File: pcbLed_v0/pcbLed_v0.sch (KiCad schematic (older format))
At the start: 16 parts, among them IC1 SN74AHCT125N, J1 Conn_01x02_Male

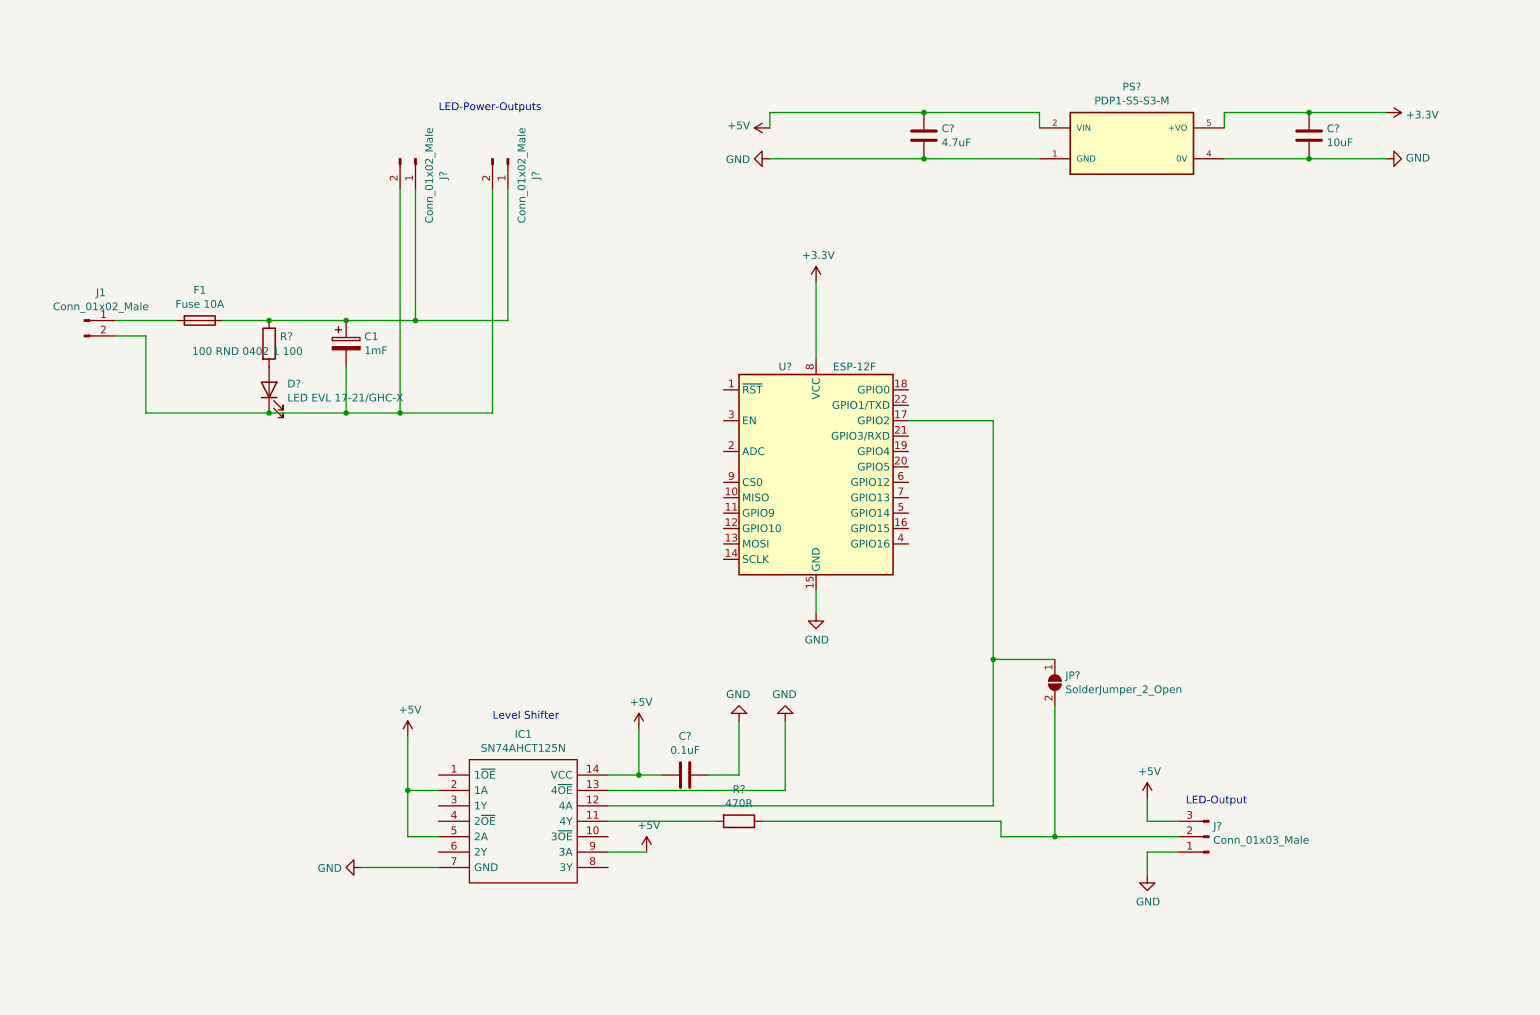
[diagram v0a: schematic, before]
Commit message: prototyp with full power supply through pcb
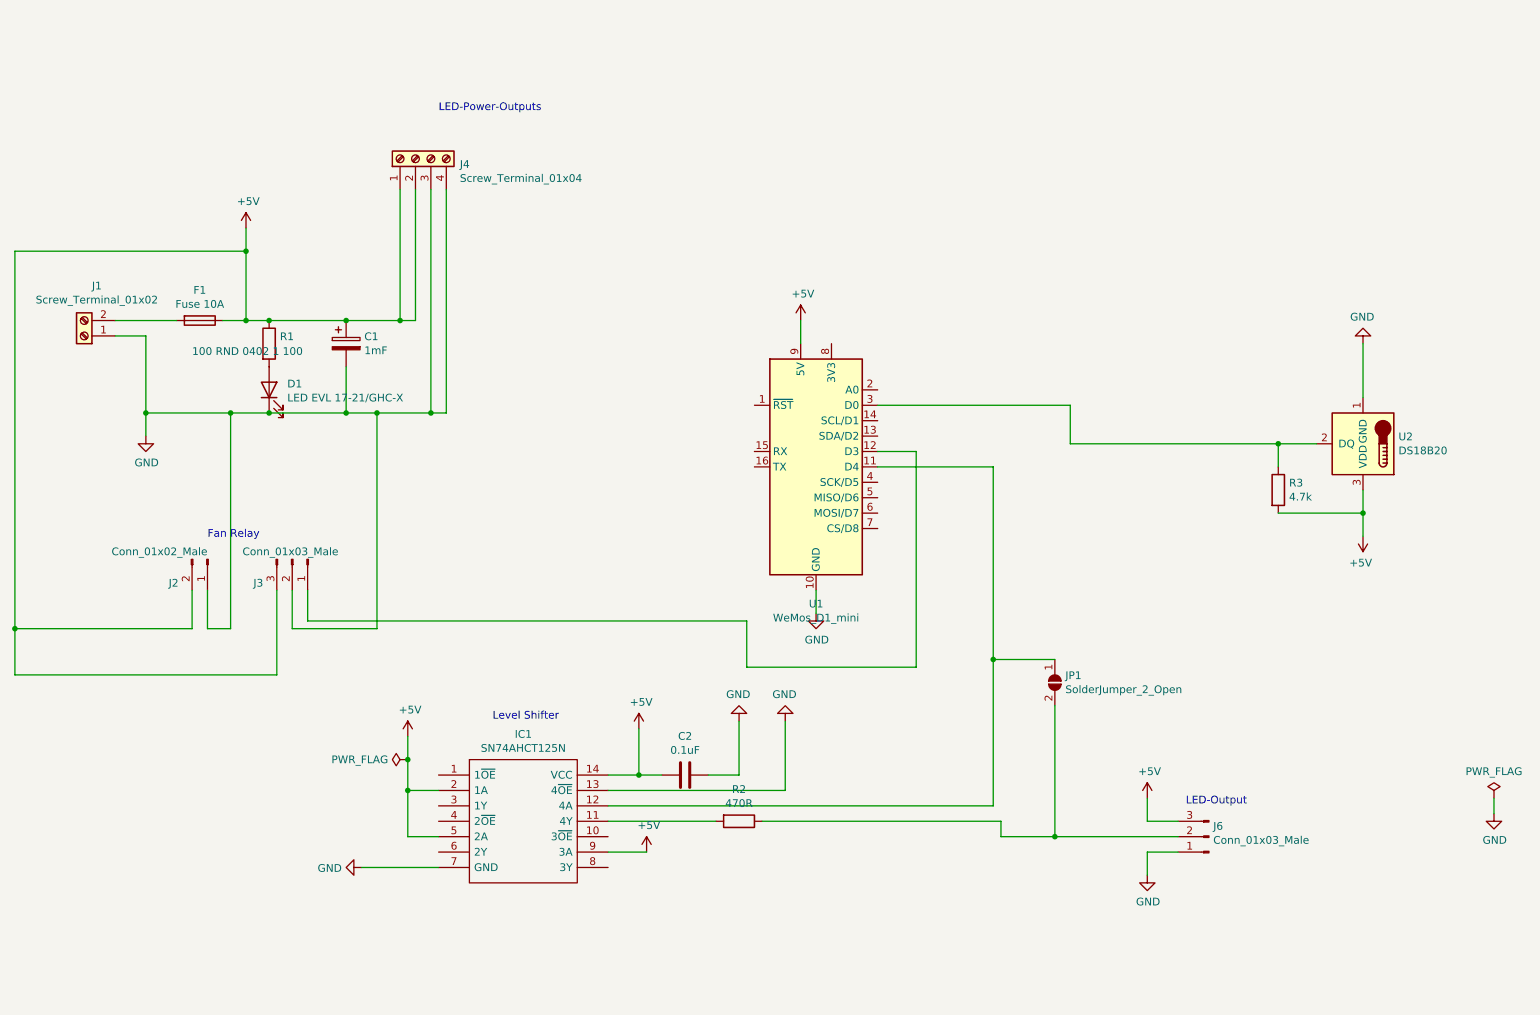
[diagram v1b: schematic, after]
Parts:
- removed C?: 4.7uF, symbol Device:C
- removed C?: 10uF, symbol Device:C
- removed J1, J? (x2): Conn_01x02_Male, symbol Connector:Conn_01x02_Male
- removed PS?: PDP1-S5-S3-M, CONV_PDP1-S5-S3-M, symbol PDP1-S5-S3-M:PDP1-S5-S3-M
- removed U?: ESP-12F, RF_Module:ESP-12E, symbol RF_Module:ESP-12F
- added J1: Screw_Terminal_01x02, TerminalBlock:TerminalBlock_Altech_AK300-2_P5.00mm, symbol Connector:Screw_Terminal_01x02
- added J2: Conn_01x02_Male, Connector_PinHeader_2.54mm:PinHeader_2x01_P2.54mm_Vertical, symbol Connector:Conn_01x02_Male
- added J3: Conn_01x03_Male, Connector_PinHeader_2.54mm:PinHeader_1x03_P2.54mm_Vertical, symbol Connector:Conn_01x03_Male
- added J4: Screw_Terminal_01x04, TerminalBlock:TerminalBlock_Altech_AK300-4_P5.00mm, symbol Connector:Screw_Terminal_01x04
- added R3: 4.7k, Resistor_SMD:R_0402_1005Metric_Pad0.72x0.64mm_HandSolder, symbol Device:R
- added U1: WeMos_D1_mini, Module:WEMOS_D1_mini_light, symbol MCU_Module:WeMos_D1_mini
- added U2: DS18B20, Package_TO_SOT_THT:TO-92_Inline, symbol Sensor_Temperature:DS18B20
- C1: footprint (none) -> Capacitor_THT:CP_Radial_D10.0mm_P5.00mm
- C2: renamed from C?; footprint (none) -> Capacitor_SMD:C_1812_4532Metric_Pad1.57x3.40mm_HandSolder
- D1: renamed from D?; footprint (none) -> LED_SMD:LED_0805_2012Metric_Pad1.15x1.40mm_HandSolder
- F1: footprint (none) -> Belfuse220043:BELFUSE220043_10A_SMD2410
- IC1: footprint DIP794W53P254L1930H508Q14N -> SamacSys_Parts:DIP794W53P254L1930H508Q14N
- J6: renamed from J?; footprint (none) -> Connector_PinHeader_2.54mm:PinHeader_1x03_P2.54mm_Vertical
- JP1: renamed from JP?; footprint (none) -> Jumper:SolderJumper-2_P1.3mm_Open_Pad1.0x1.5mm
- R1, R2: renamed from R?; footprint (none) -> Resistor_SMD:R_0402_1005Metric_Pad0.72x0.64mm_HandSolder
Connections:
- net +5V: now also C1.1, F1.1, R1.1, J2.2 (Pin_2), J3.3 (Pin_3), J4.1 (Pin_1), J4.2 (Pin_2), R3.2, U1.9 (5V), U2.3 (VDD)
- net GND: now also C1.2, D1.1 (K), J1.1 (Pin_1), J2.1 (Pin_1), J3.2 (Pin_2), J4.3 (Pin_3), J4.4 (Pin_4), U1.10 (GND), U2.1 (GND)
- net at IC1.12 (4A), JP1.1 (A): now also U1.11 (D4)
- net at F1.2: now also J1.2 (Pin_2)
- new net: R3.1, U1.3 (D0), U2.2 (DQ)
- new net: J3.1 (Pin_1), U1.12 (D3)
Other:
- note added: "Fan Relay\n\n"

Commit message: split to 2 pcbs; one for power supply; one for the other
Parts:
- removed C1: 1mF, Capacitor_THT:CP_Radial_D10.0mm_P5.00mm, symbol Device:CP
- removed D1: LED EVL 17-21/GHC-X, LED_SMD:LED_0805_2012Metric_Pad1.15x1.40mm_HandSolder, symbol Device:LED
- removed F1: Fuse 10A, Belfuse220043:BELFUSE220043_10A_SMD2410, symbol Device:Fuse
- removed J1: Screw_Terminal_01x02, TerminalBlock:TerminalBlock_Altech_AK300-2_P5.00mm, symbol Connector:Screw_Terminal_01x02
- removed J4: Screw_Terminal_01x04, TerminalBlock:TerminalBlock_Altech_AK300-4_P5.00mm, symbol Connector:Screw_Terminal_01x04
- added H1, H2, H3, H4: MountingHole, MountingHole:MountingHole_3.2mm_M3_DIN965, symbol Mechanical:MountingHole
- added J3: Conn_01x03_Male, Connector_PinHeader_2.54mm:PinHeader_1x03_P2.54mm_Vertical, symbol Connector:Conn_01x03_Male
- added JP1: SolderJumper_2_Open, Jumper:SolderJumper-2_P1.3mm_Open_Pad1.0x1.5mm, symbol Jumper:SolderJumper_2_Open
- R1: value 100 RND 0402 1 100 -> 470R
- renumbered C2 to C1, J2 to J1, J3 to J2, J6 to J4, JP1 to JP2
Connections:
- net +5V: now also J3.3 (Pin_3); no longer IC1.9 (3A), R1.1
- net GND: now also J3.1 (Pin_1)
- net at R1.2: now also IC1.8 (3Y)
- net D1: now reaches U1.14 (SCL/D1)
- net D1: now also IC1.9 (3A), JP1.1 (A)
- new net: J3.2 (Pin_2), JP1.2 (B), R1.1
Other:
- note removed: "LED-Power-Outputs\n"
